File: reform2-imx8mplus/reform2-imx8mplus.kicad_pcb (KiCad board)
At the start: 6 copper layers, 47 x 67.8 mm, 7 parts, among them J1 Conn_01x33, U1 reform2-som-connector, U2 Nit8M_Plus_SOM_J5, U3 Nit8M_Plus_SOM_J4, U4 Nit8M_Plus_SOM_J8

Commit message: imx8mplus: first rev routed
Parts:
- added C1: 1uF, Capacitor_SMD:C_0603_1608Metric, F.Cu at (138.8, 76.0)
- added G***: LOGO, footprints:mntreform, F.Cu at (120.9, 72.2)
- added J2: Conn_01x06, Connector_PinHeader_2.00mm:PinHeader_1x06_P2.00mm_Vertical, F.Cu at (122.7, 66.0)
- added R3: 1k, Capacitor_SMD:C_0603_1608Metric, F.Cu at (145.5, 72.9)
- added R4: 0, Capacitor_SMD:C_0603_1608Metric, F.Cu at (123.5, 69.2)
- added SW1: SW_SPST, Connector_PinHeader_2.00mm:PinHeader_1x02_P2.00mm_Horizontal, F.Cu at (148.0, 89.8)
- added TP1: TP_USB1_ID, TestPoint:TestPoint_Pad_1.0x1.0mm, F.Cu at (130.5, 126.5)
- added TP2: TP_USB2_ID, TestPoint:TestPoint_Pad_1.0x1.0mm, F.Cu at (128.0, 126.5)
- added TP3: TP_ONOFF, TestPoint:TestPoint_Pad_1.0x1.0mm, F.Cu at (145.7, 76.4)
- added TP4: TP_ONREQ, TestPoint:TestPoint_Pad_1.0x1.0mm, F.Cu at (145.7, 78.9)
- added U5: NCP718xSN330, Package_TO_SOT_SMD:SOT-23-5, F.Cu at (141.7, 73.9)
- moved R1 61.0 mm to (106.0, 84.5), turned to 180 degrees
- moved R2 58.2 mm to (106.0, 86.0), turned to 180 degrees
- moved J1 2.76 mm to (135.9, 67.5)
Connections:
- U2 pad 17: unconnected-(U2-Pad17) -> BOOT_MODE1
- U3 pad 64: unconnected-(U3-Pad64) -> USB1_VBUS_3V3
- U3 pad 66: unconnected-(U3-Pad66) -> Net-(U3-Pad66)
- U3 pad 69: unconnected-(U3-Pad69) -> USB1_VBUS_3V3
- U3 pad 71: unconnected-(U3-Pad71) -> Net-(U3-Pad71)
- U3 pad 87: unconnected-(U3-Pad87) -> GPIO1_IO12
- U3 pad 90: unconnected-(U3-Pad90) -> GPIO1_IO09
- U3 pad 93: unconnected-(U3-Pad93) -> GPIO1_IO14
- U3 pad 95: unconnected-(U3-Pad95) -> GND
- U3 pad 97: SD2_CD -> GPIO1_IO05
- U4 pad 33: unconnected-(U4-Pad33) -> Net-(U4-Pad33)
- U4 pad 34: unconnected-(U4-Pad34) -> Net-(U4-Pad34)
- U4 pad 35: unconnected-(U4-Pad35) -> Net-(U4-Pad35)
- U4 pad 36: unconnected-(U4-Pad36) -> Net-(U4-Pad36)
- U4 pad 38: unconnected-(U4-Pad38) -> Net-(U4-Pad38)
- U4 pad 40: unconnected-(U4-Pad40) -> Net-(U4-Pad40)
- U4 pad 42: unconnected-(U4-Pad42) -> Net-(U4-Pad42)
- U4 pad 45: unconnected-(U4-Pad45) -> CLKIN1
- U4 pad 46: unconnected-(U4-Pad46) -> Net-(U4-Pad46)
- U4 pad 48: unconnected-(U4-Pad48) -> SD2_RESET
- U4 pad 49: unconnected-(U4-Pad49) -> CLKOUT1
- U4 pad 53: unconnected-(U4-Pad53) -> CLKIN2
- U4 pad 57: unconnected-(U4-Pad57) -> CLKOUT2
- U4 pad 68: unconnected-(U4-Pad68) -> SD2_DATA4
- U4 pad 70: unconnected-(U4-Pad70) -> SD2_DATA5
- U4 pad 72: unconnected-(U4-Pad72) -> SD2_DATA6
- U4 pad 74: unconnected-(U4-Pad74) -> SD2_DATA7
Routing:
- net GND: track 0.00 -> 251.6 mm, vias 0 -> 121
- net +5V: track 0.00 -> 184.3 mm, vias 0 -> 3
- net HDMI_TX2_P: track 0.00 -> 77.9 mm
- net HDMI_TX2_N: track 0.00 -> 76.6 mm
- net HDMI_TX1_P: track 0.00 -> 73.6 mm
- net HDMI_TX1_N: track 0.00 -> 72.2 mm
- net HDMI_TX0_P: track 0.00 -> 69.3 mm
- net HDMI_TX0_N: track 0.00 -> 68.0 mm
- net USB1_VBUS_3V3: track 0.00 -> 66.5 mm, vias 0 -> 2
- net HDMI_CLK_P: track 0.00 -> 65.2 mm
- net IMX_RESETn: track 0.00 -> 64.3 mm, vias 0 -> 2
- net HDMI_CLK_N: track 0.00 -> 63.9 mm
- net HDMI_DDC_SDA: track 0.00 -> 58.2 mm, vias 0 -> 2
- net HDMI_DDC_SCL: track 0.00 -> 57.5 mm, vias 0 -> 2
- net HDMI_HPD: track 0.00 -> 57.2 mm, vias 0 -> 2
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- added copper zone on B.Cu, net GND
- added copper zone on F.Cu, net GND
- added copper zone on In1.Cu, net GND
- added copper zone on In2.Cu, net GND
- added copper zone on In3.Cu, net GND
- added copper zone on In4.Cu, net GND
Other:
- board size 47 x 67.8 mm -> 50 x 67.8 mm

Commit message: imx8mplus: moved some things around; final tweaks and export for first test order
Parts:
- added GFX2: Badge, footprints:reform2-imx8mplus-badge, F.Cu at (119.9, 120.0)
- added H1: MountingHole_Pad, MountingHole:MountingHole_2.2mm_M2_DIN965_Pad, F.Cu at (144.2, 63.8)
- added H2: MountingHole_Pad, MountingHole:MountingHole_2.2mm_M2_DIN965_Pad, F.Cu at (144.2, 123.8)
- added H3: MountingHole_Pad, MountingHole:MountingHole_2.2mm_M2_DIN965_Pad, F.Cu at (135.9, 101.0)
- GFX1: renamed from G***; value LOGO -> Logo
- moved J1 13.5 mm to (146.0, 76.4), turned to 90 degrees
- moved TP3 12.9 mm to (138.5, 65.7)
- moved TP4 12.9 mm to (138.5, 68.2)
- moved C1 12.1 mm to (131.3, 66.5)
- moved U5 12.1 mm to (134.2, 64.4)
- moved R3 12.0 mm to (138.1, 63.4)
- moved J2 3.40 mm to (126.0, 66.8)
- moved R4 1.49 mm to (124.9, 69.7), turned to 0 degrees
- moved GFX1 0.30 mm to (120.6, 72.2)
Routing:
- net +5V: track 184.3 -> 143.5 mm
- net USB1_VBUS_3V3: track 66.5 -> 79.5 mm
- net DSI1_D3_P: track 40.9 -> 48.1 mm
- net TRX0_P: track 27.4 -> 34.0 mm
- net TRX0_N: track 28.1 -> 34.7 mm
- net DSI1_D2_P: track 41.8 -> 48.2 mm
- net DSI1_D3_N: track 41.6 -> 47.9 mm
- net DSI1_D2_N: track 42.5 -> 48.2 mm
- net DSI1_C_P: track 42.7 -> 48.2 mm
- net DSI1_C_N: track 43.4 -> 48.2 mm
- net DSI1_D1_P: track 43.8 -> 48.1 mm
- net DSI1_D0_P: track 45.0 -> 48.5 mm
- net DSI1_D1_N: track 44.5 -> 48.0 mm
- net DSI1_D0_N: track 45.6 -> 48.5 mm
- net GND: track 251.6 -> 248.8 mm, vias 121 -> 193
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
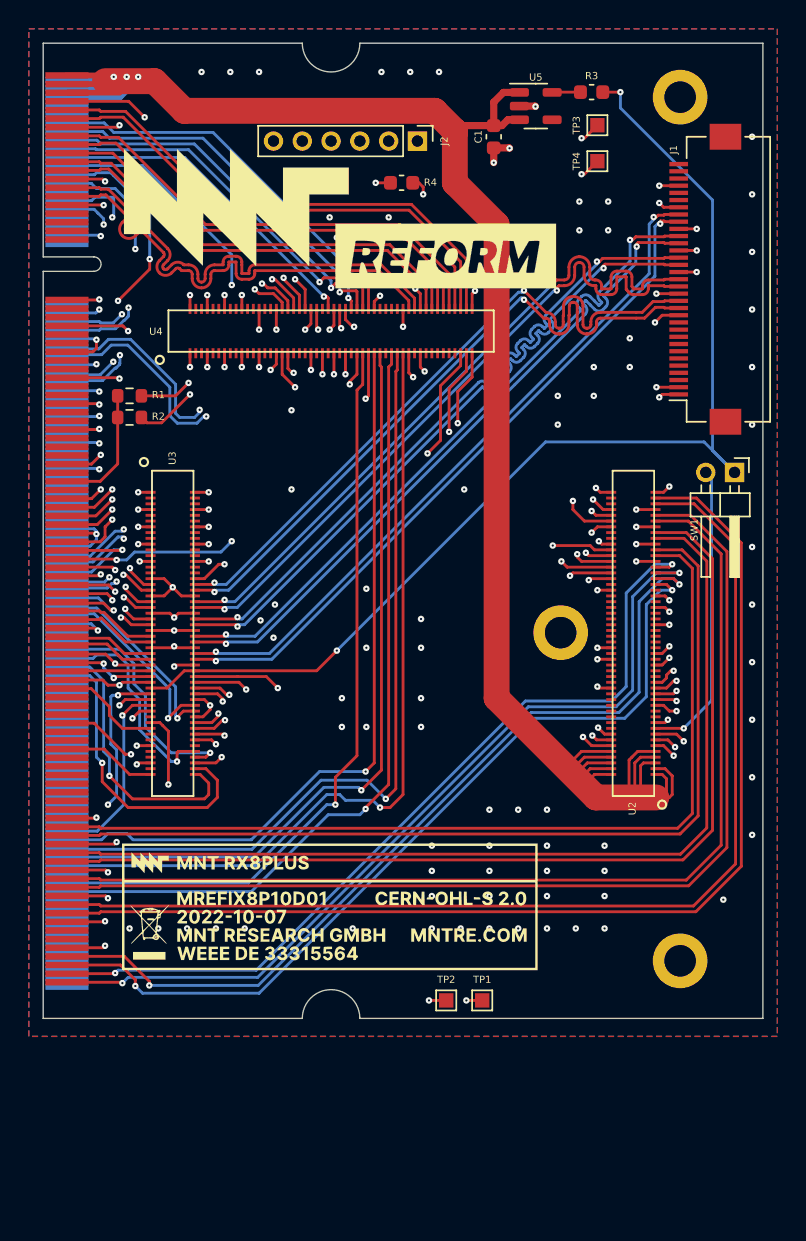
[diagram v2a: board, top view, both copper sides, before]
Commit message: imx8mplus: last minute diff pair length tuning
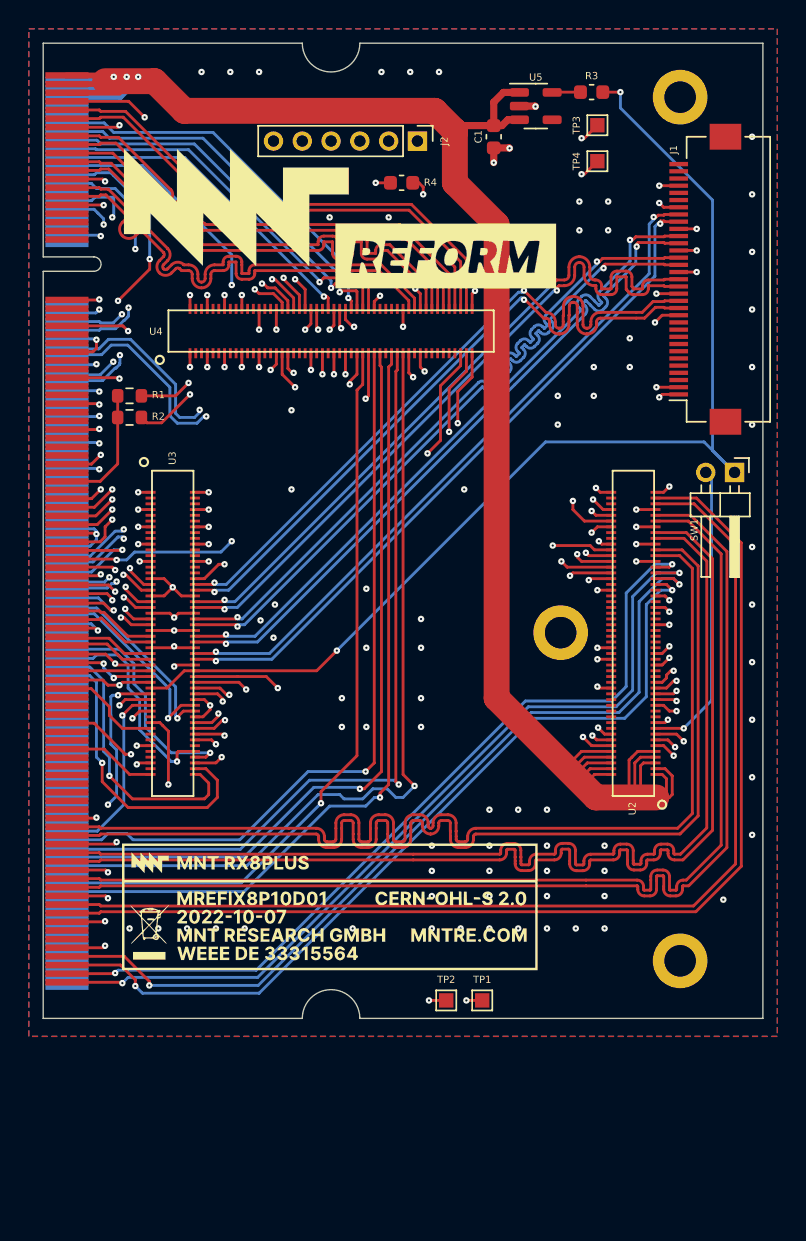
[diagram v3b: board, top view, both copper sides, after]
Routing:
- net HDMI_CLK_P: track 65.2 -> 76.8 mm
- net HDMI_CLK_N: track 63.9 -> 75.4 mm
- net HDMI_TX0_N: track 68.0 -> 75.5 mm
- net HDMI_TX0_P: track 69.3 -> 76.8 mm
- net TRX1_P: track 29.8 -> 33.7 mm
- net TRX1_N: track 30.5 -> 34.3 mm
- net GND: track 248.8 -> 245.4 mm, vias 193 -> 192
- net HDMI_TX1_N: track 72.2 -> 75.5 mm
- net HDMI_TX1_P: track 73.6 -> 76.8 mm
- net TRX2_P: track 32.3 -> 34.4 mm
- net TRX2_N: track 33.0 -> 35.1 mm
- net DAC_TXFS: track 56.8 -> 57.6 mm
- net DAC_RXFS: track 56.0 -> 55.3 mm
- net DAC_MCLK: track 53.1 -> 52.4 mm

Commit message: imx8mplus: correct the mezzanine footprint, reroute everything, d-2 off to fab
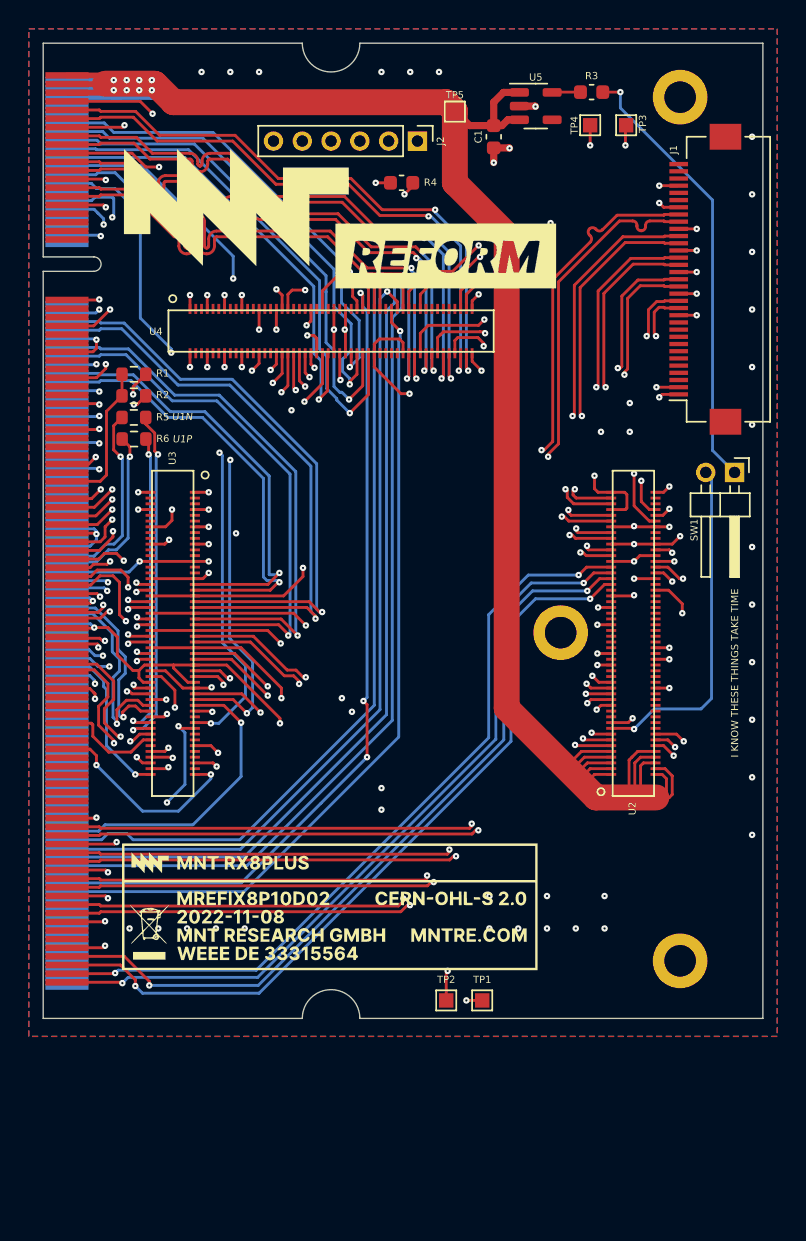
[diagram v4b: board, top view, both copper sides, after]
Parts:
- added R5: 0, Resistor_SMD:R_0603_1608Metric, F.Cu at (106.3, 86.0)
- added R6: 0, Resistor_SMD:R_0603_1608Metric, F.Cu at (106.3, 87.5)
- added TP5: TP_5V, TestPoint:TestPoint_Pad_1.0x1.0mm, F.Cu at (128.6, 64.8)
- moved TP4 2.55 mm to (138.0, 65.7)
- moved TP3 2.00 mm to (140.5, 65.7)
- moved R1 1.53 mm to (106.3, 83.0)
- moved R2 1.53 mm to (106.3, 84.5)
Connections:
- U1 pad 100: USB1_N -> Net-(U1-Pad100)
- U1 pad 102: USB1_P -> Net-(U1-Pad102)
- U1 pad 123: GND -> unconnected-(U1-Pad123)
- U1 pad 129: GND -> unconnected-(U1-Pad129)
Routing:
- net GND: track 245.4 -> 312.8 mm, vias 192 -> 152
- net USB2_TX_P: track 6.54 -> 30.7 mm, vias 0 -> 2
- net USB2_TX_N: track 6.54 -> 29.9 mm, vias 0 -> 2
- net USB2_P: track 5.83 -> 26.5 mm, vias 0 -> 2
- net USB2_N: track 6.47 -> 25.2 mm
- net LPC_UART_RX: track 48.7 -> 65.2 mm
- net USB2_RX_N: track 6.29 -> 22.5 mm, vias 0 -> 2
- net LPC_SSO: track 42.4 -> 58.5 mm
- net LPC_UART_TX: track 48.4 -> 64.5 mm
- net USB2_RX_P: track 6.29 -> 22.3 mm, vias 0 -> 2
- net HDMI_TX2_P: track 77.9 -> 63.4 mm, vias 0 -> 2
- net HDMI_TX1_P: track 76.8 -> 63.3 mm, vias 0 -> 2
- net HDMI_CLK_P: track 76.8 -> 63.3 mm, vias 0 -> 2
- net HDMI_TX0_P: track 76.8 -> 63.3 mm, vias 0 -> 2
- net USB_HUB_RESET: track 7.30 -> 20.7 mm, vias 0 -> 3
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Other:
- board text added: "I KNOW THESE THINGS TAKE TIME"
- board text added: "U1N"
- board text added: "U1P"

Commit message: imx8mplus: change drill size to 0.2mm, add optional 3v3 source via reset pin
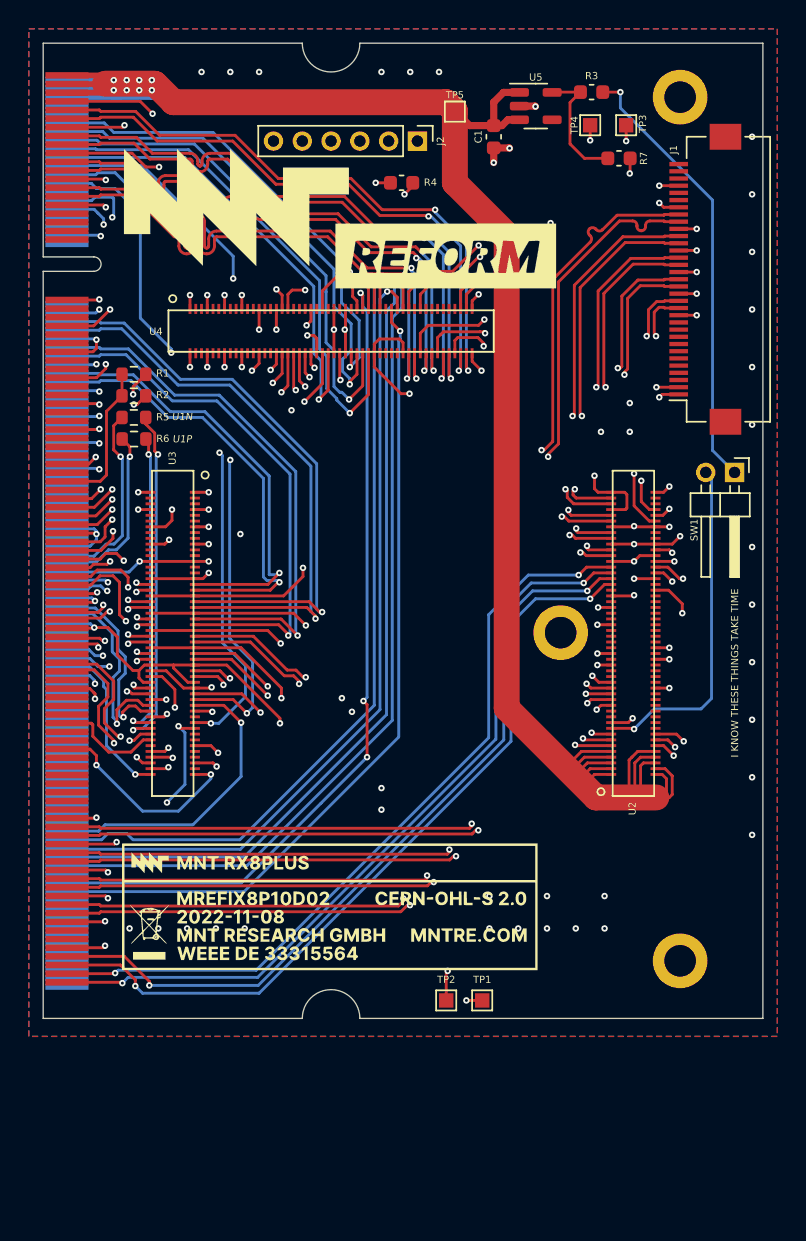
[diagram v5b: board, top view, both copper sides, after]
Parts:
- added R7: 1k, Capacitor_SMD:C_0603_1608Metric, F.Cu at (140.0, 68.0)
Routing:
- net IMX_RESETn: track 67.5 -> 97.0 mm, vias 2 -> 3
- net +3V3: track 1.98 -> 8.92 mm
